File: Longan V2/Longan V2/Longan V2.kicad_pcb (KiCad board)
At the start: 2 copper layers, 37.5 x 54 mm, 17 parts, among them J1 Conn_Coaxial, J2 Conn_Coaxial, J3 Conn_02x09_Odd_Even, J5 Battery, J6 Serial Output, SW1 Reset SW, U1 Ai-Thinker-Ra-01, U2 MAX-M8Q, U3 Pico

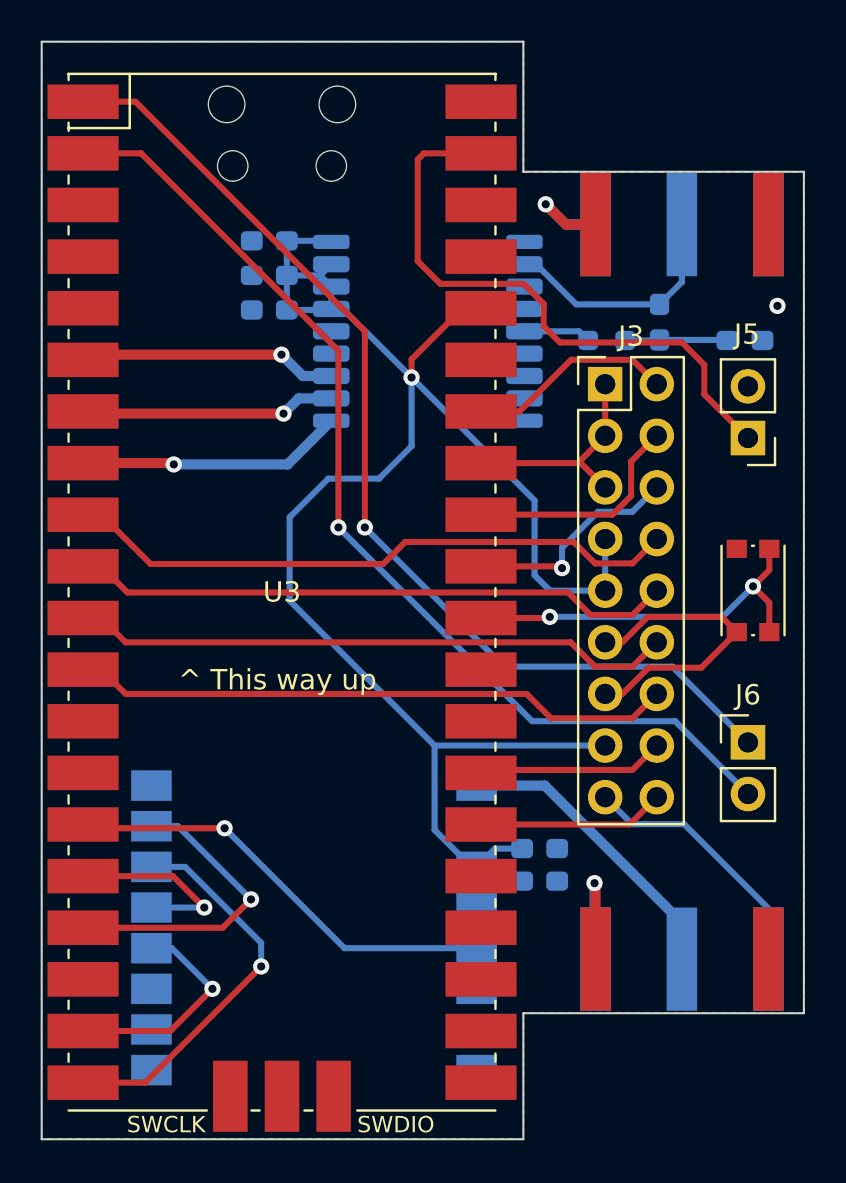
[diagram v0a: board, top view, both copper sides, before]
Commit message: Polishing
- More vias
- Test points
- Narrower zones
- Logo
- Pin Labels
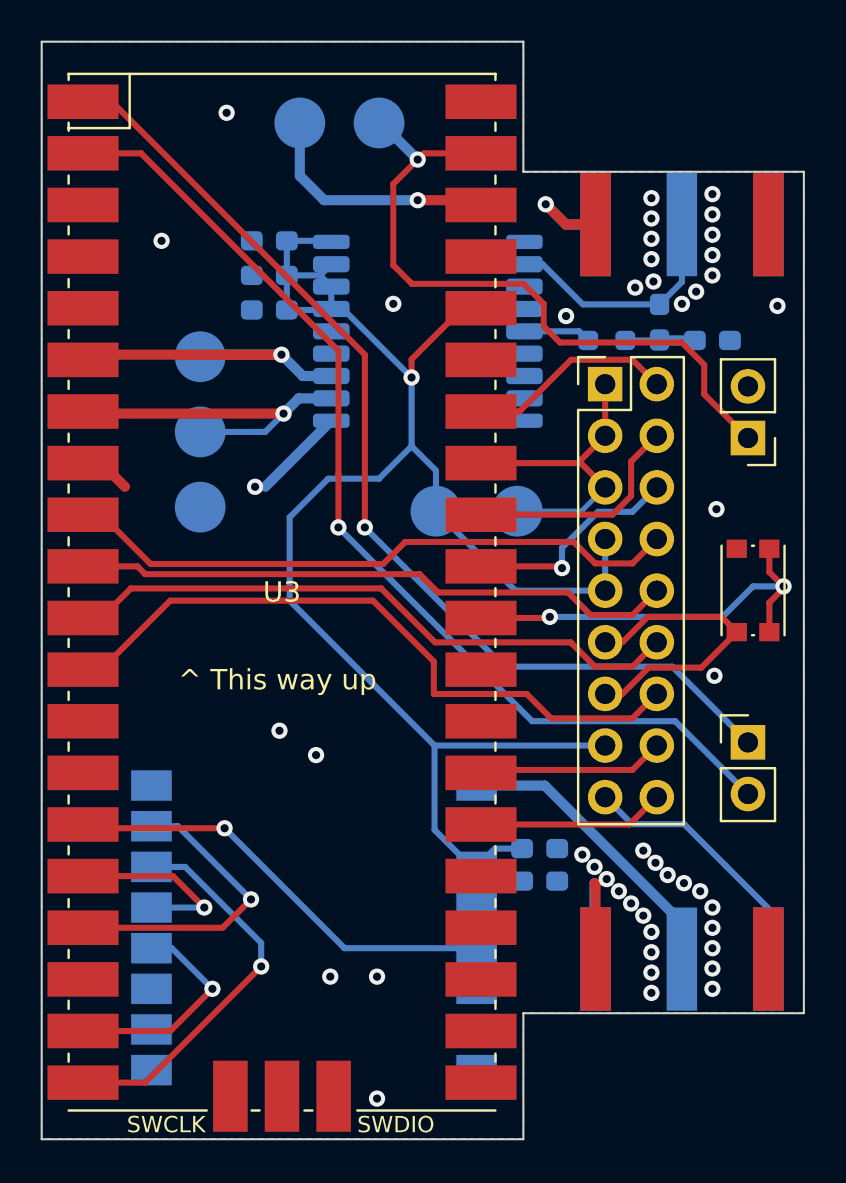
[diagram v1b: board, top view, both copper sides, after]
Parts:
- added 3v3: 3v3, TestPoint:TestPoint_Pad_D2.5mm, B.Cu at (157.4, 94.1)
- added BAT: Bat, TestPoint:TestPoint_Pad_D2.5mm, B.Cu at (154.6, 75.0)
- added G***: LOGO_ICON, CUSF Silks:CUSF_Logo_Icon, B.Cu at (140.9, 97.4)
- added GND: GND, TestPoint:TestPoint_Pad_D2.5mm, B.Cu at (145.8, 93.9)
- added GND: GND, TestPoint:TestPoint_Pad_D2.5mm, B.Cu at (150.7, 75.0)
- added GNDA: GNDA, TestPoint:TestPoint_Pad_D2.5mm, B.Cu at (161.4, 94.1)
- added RX: GPS_RX, TestPoint:TestPoint_Pad_D2.5mm, B.Cu at (145.8, 90.2)
- added TX: GPS_TX, TestPoint:TestPoint_Pad_D2.5mm, B.Cu at (145.8, 86.5)
- moved C3 1.60 mm to (171.0, 85.7)
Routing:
- net GND: track 51.0 -> 56.3 mm, vias 4 -> 48
- net GNDA: track 11.9 -> 16.7 mm
- net /RX_1: track 11.7 -> 16.1 mm
- net /BAT_IN: track 28.7 -> 33.1 mm, vias 0 -> 1
- net /TX_1: track 11.9 -> 15.9 mm
- net /GPIO_4: track 28.8 -> 32.6 mm
- net +3V3: track 85.2 -> 82.8 mm
- net Net-(C3-Pad2): track 5.05 -> 3.45 mm
- net Net-(SW1-Pad1): track 19.7 -> 21.1 mm
- net /GPIO_3: track 28.8 -> 30.0 mm
- net /TX_0: track 50.5 -> 49.9 mm
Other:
- board text added: "3v3"
- board text added: "ANT"
- board text added: "Cambridge University Spaceflight 2022 Designed by W. Yu Made in Cambridge, UK"
- board text added: "GND"
- board text added: "LONGAN V2"
